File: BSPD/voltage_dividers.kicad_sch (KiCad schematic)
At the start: 10 parts

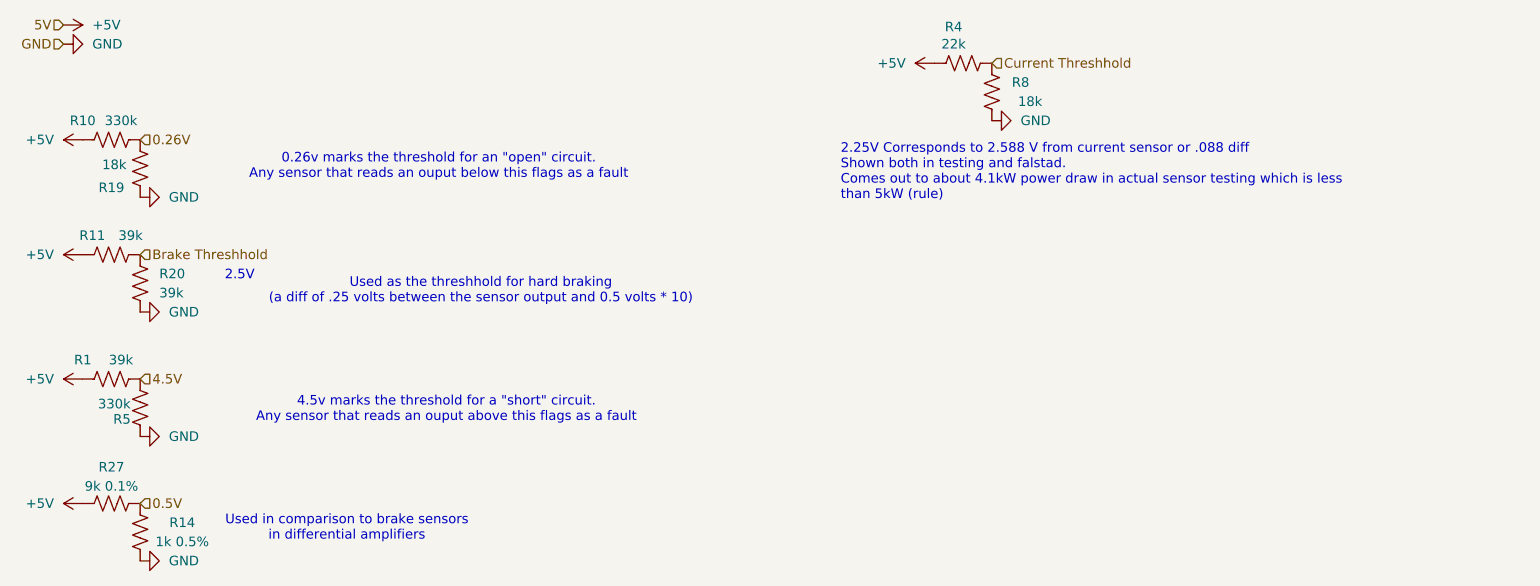
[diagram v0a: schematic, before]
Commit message: Overhaul of BPSD to V3.0
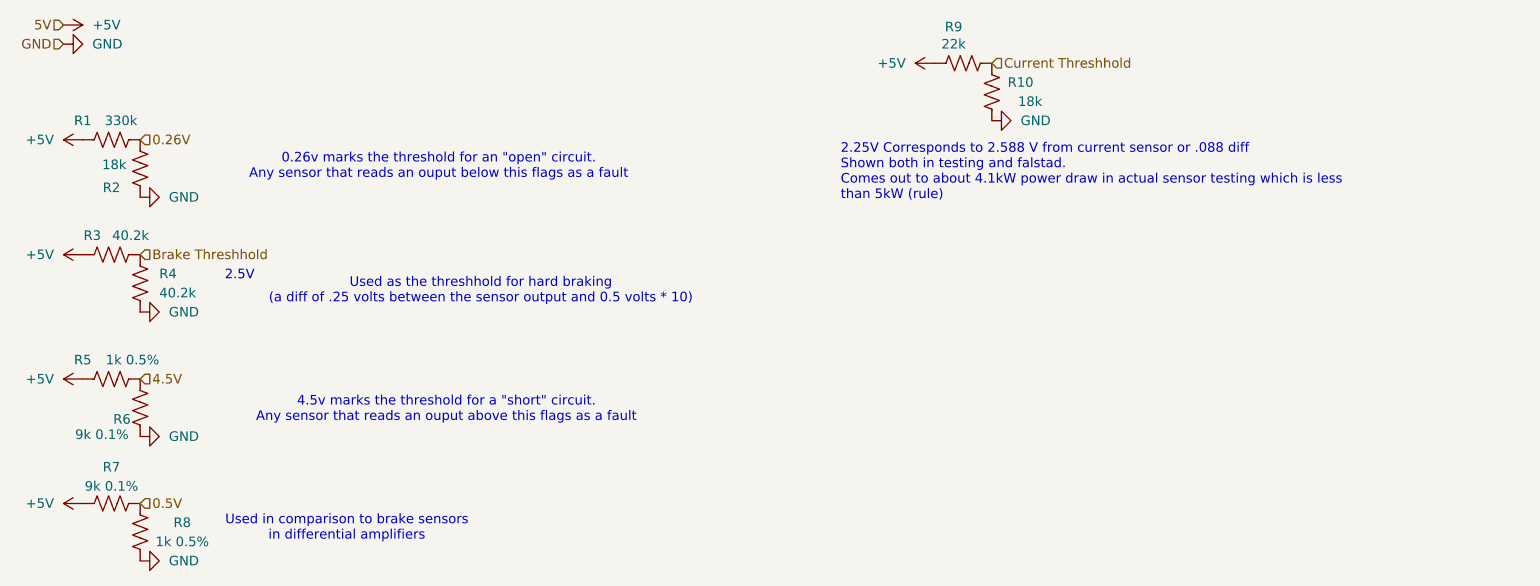
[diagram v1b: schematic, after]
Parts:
- R3: renamed from R11; value 39k -> 40.2k
- R4: renamed from R20; value 39k -> 40.2k
- R5: renamed from R1; value 39k -> 1k 0.5%
- R6: renamed from R5; value 330k -> 9k 0.1%
- renumbered R10 to R1, R8 to R10, R19 to R2, R27 to R7, R14 to R8, R4 to R9
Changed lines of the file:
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@@
 		(on_board yes)
 		(dnp no)
-		(property "Reference" "R5"
+		(property "Reference" "R6"
 			(at 26.797 66.294 0)
 			(effects
@@
 			)
 		)
-		(property "Value" "330k"
-			(at 25.781 64.262 0)
+		(property "Value" "9k 0.1%"
+			(at 24.13 68.326 0)
 			(effects
 				(font
@@
 			(project "BSPD"
 				(path "/9b958334-fa88-4811-8197-71444a07b1b5/72204750-f360-4c1a-afa5-7db4b1bb107e"
-					(reference "R5")
+					(reference "R6")
 					(unit 1)
 				)
@@
 		(on_board yes)
 		(dnp no)
-		(property "Reference" "R1"
+		(property "Reference" "R5"
 			(at 21.59 58.42 90)
 			(effects
@@
 			)
 		)
-		(property "Value" "39k"
-			(at 26.67 58.42 90)
+		(property "Value" "1k 0.5%"
+			(at 28.194 58.42 90)
 			(effects
 				(font
@@
 			(project "BSPD"
 				(path "/9b958334-fa88-4811-8197-71444a07b1b5/72204750-f360-4c1a-afa5-7db4b1bb107e"
-					(reference "R1")
+					(reference "R5")
 					(unit 1)
 				)
@@
 		(on_board yes)
 		(dnp no)
-		(property "Reference" "R19"
+		(property "Reference" "R2"
 			(at 25.4 35.56 0)
 			(effects
@@
 			(project "BSPD"
 				(path "/9b958334-fa88-4811-8197-71444a07b1b5/72204750-f360-4c1a-afa5-7db4b1bb107e"
-					(reference "R19")
+					(reference "R2")
 					(unit 1)
 				)
@@
 		(on_board yes)
 		(dnp no)
-		(property "Reference" "R14"
+		(property "Reference" "R8"
 			(at 34.798 80.01 0)
 			(effects
@@
 			(project "BSPD"
 				(path "/9b958334-fa88-4811-8197-71444a07b1b5/72204750-f360-4c1a-afa5-7db4b1bb107e"
-					(reference "R14")
+					(reference "R8")
 					(unit 1)
 				)
@@
 		(on_board yes)
 		(dnp no)
-		(property "Reference" "R10"
+		(property "Reference" "R1"
 			(at 21.59 26.67 90)
 			(effects
@@
 			(project "BSPD"
 				(path "/9b958334-fa88-4811-8197-71444a07b1b5/72204750-f360-4c1a-afa5-7db4b1bb107e"
-					(reference "R10")
+					(reference "R1")
 					(unit 1)
 				)
@@
 		(on_board yes)
 		(dnp no)
-		(property "Reference" "R4"
+		(property "Reference" "R9"
 			(at 137.16 14.224 90)
 			(effects
@@
 			(project "BSPD"
 				(path "/9b958334-fa88-4811-8197-71444a07b1b5/72204750-f360-4c1a-afa5-7db4b1bb107e"
-					(reference "R4")
+					(reference "R9")
 					(unit 1)
 				)
@@
 		(on_board yes)
 		(dnp no)
-		(property "Reference" "R27"
+		(property "Reference" "R7"
 			(at 25.4 72.644 90)
 			(effects
@@
 			(project "BSPD"
 				(path "/9b958334-fa88-4811-8197-71444a07b1b5/72204750-f360-4c1a-afa5-7db4b1bb107e"
-					(reference "R27")
+					(reference "R7")
 					(unit 1)
 				)
@@
 		(dnp no)
 		(fields_autoplaced yes)
-		(property "Reference" "R20"
+		(property "Reference" "R4"
 			(at 31.75 46.9899 0)
 			(effects
@@
 			)
 		)
-		(property "Value" "39k"
+		(property "Value" "40.2k"
 			(at 31.75 49.5299 0)
 			(effects
@@
 			(project "BSPD"
 				(path "/9b958334-fa88-4811-8197-71444a07b1b5/72204750-f360-4c1a-afa5-7db4b1bb107e"
-					(reference "R20")
+					(reference "R4")
 					(unit 1)
 				)
@@
 		(on_board yes)
 		(dnp no)
-		(property "Reference" "R8"
+		(property "Reference" "R10"
 			(at 146.05 21.59 0)
 			(effects
@@
 			(project "BSPD"
 				(path "/9b958334-fa88-4811-8197-71444a07b1b5/72204750-f360-4c1a-afa5-7db4b1bb107e"
-					(reference "R8")
+					(reference "R10")
 					(unit 1)
 				)
@@
 		(on_board yes)
 		(dnp no)
-		(property "Reference" "R11"
+		(property "Reference" "R3"
 			(at 22.86 41.91 90)
 			(effects
@@
 			)
 		)
-		(property "Value" "39k"
+		(property "Value" "40.2k"
 			(at 27.94 41.91 90)
 			(effects
@@
 			(project "BSPD"
 				(path "/9b958334-fa88-4811-8197-71444a07b1b5/72204750-f360-4c1a-afa5-7db4b1bb107e"
-					(reference "R11")
-					(unit 1)
-				)
+					(reference "R3")
+					(unit 1)
+				)
